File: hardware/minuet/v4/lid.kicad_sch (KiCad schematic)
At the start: 13 parts, among them J9 B2B-XH-A, U6 DRV8876PWP

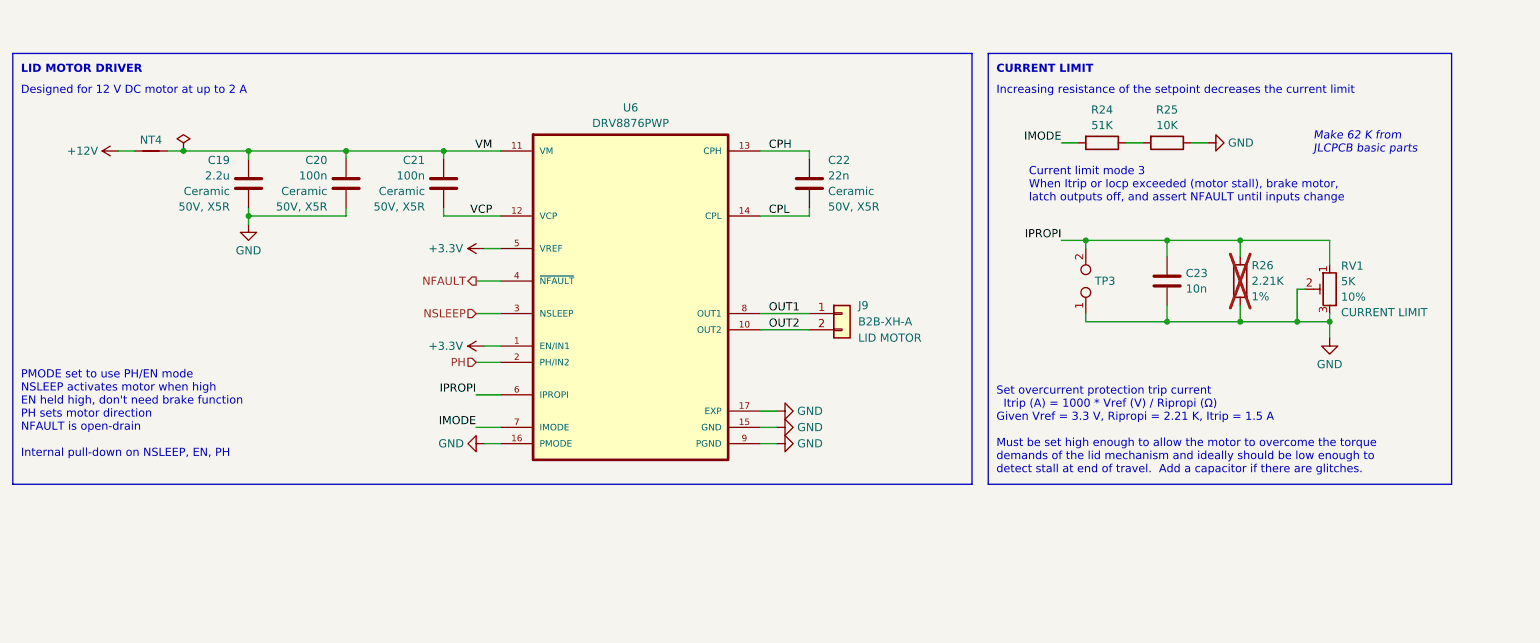
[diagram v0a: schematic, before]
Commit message: First draft of Minuet v4 fan controller board
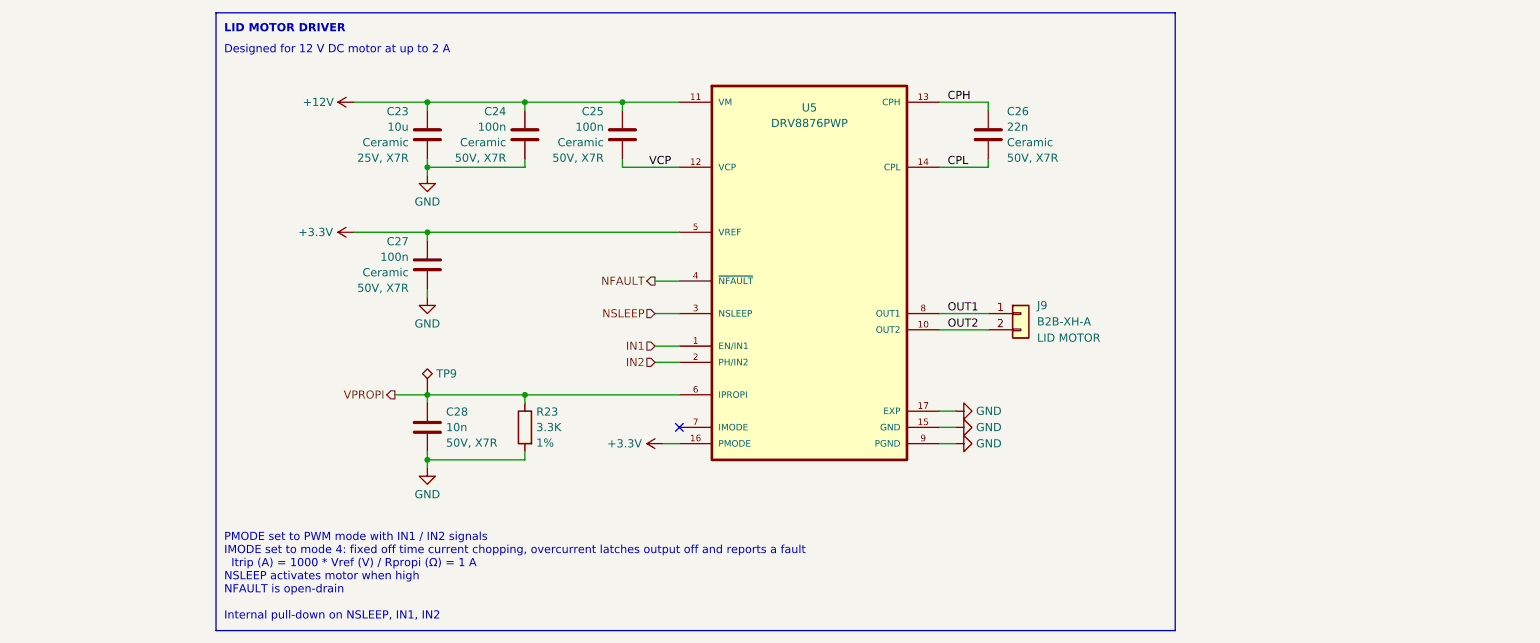
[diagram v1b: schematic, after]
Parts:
- removed C19: 2.2u, Capacitor_SMD:C_0805_2012Metric, symbol Device:C
- removed NT4: NetTie_2, Generic:NetTie-2_SMD_Pad1.0mm, symbol Device:NetTie_2
- removed R24: 51K, Resistor_SMD:R_0603_1608Metric, symbol Device:R
- removed R25: 10K, Resistor_SMD:R_0603_1608Metric, symbol Device:R
- removed RV1: 5K, 3362P-1-502LF:TRIM_3362P-1-502LF, symbol Device:R_Potentiometer_Trim
- removed TP3: TestPoint_2Pole, TestPoint:TestPoint_2Pads_Pitch2.54mm_Drill0.8mm, symbol Connector:TestPoint_2Pole
- added C23: 10u, Capacitor_SMD:C_1210_3225Metric, symbol Device:C
- added C27: 100n, Capacitor_SMD:C_0603_1608Metric, symbol Device:C
- added TP9: TestPoint_Alt, TestPoint:TestPoint_Pad_D1.0mm, symbol Connector:TestPoint_Alt
- C24: renamed from C20; Rating 50V, X5R -> 50V, X7R
- C25: renamed from C21; Rating 50V, X5R -> 50V, X7R
- C26: renamed from C22; Rating 50V, X5R -> 50V, X7R
- C28: renamed from C23; Rating 50V, X5R -> 50V, X7R
- R23: renamed from R26; value 2.21K -> 3.3K; LCSC (none) -> C22978; now fitted; now in the parts list
- U5: renamed from U6; MANUFACTURER (none) -> Texas Instruments; MAXIMUM_PACKAGE_HEIGHT (none) -> 1.2mm; PACKAGE (none) -> HTSSOP-16 Texas Instruments; PARTREV (none) -> E; STANDARD (none) -> Manufacturer Recommendations
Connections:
- net VM is gone; now on net +12V: C24.1, C25.1, U5.11 (VM)
- net +12V: now also C23.1
- net +3.3V: now also U5.16 (PMODE), C27.1; no longer U5.1 (EN/IN1)
- net GND: now also C23.2, C27.2; no longer U5.16 (PMODE)
- net IMODE: no longer names the net of U5.7 (IMODE)
- net IPROPI renamed VPROPI
- net VPROPI: now also TP9.1
- net PH renamed IN2
- new net IN1: U5.1 (EN/IN1)
- no-connect marks 0 -> 1
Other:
- note added: "PMODE set to PWM mode with IN1 / IN2 signals IMODE set to mode 4: fixed off time current chopping, overcurrent latches output off and reports a fault Itrip (A) = 1000 * Vref (V) / Rpropi (Ω) = 1 A NSLEEP activates motor when high NFAULT is open-drain Internal pull-down on NSLEEP, IN1, IN2"
- note removed: "CURRENT LIMIT"
- note removed: "Current limit mode 3 When Itrip or Iocp exceeded (motor stall), brake motor, latch outputs off, and assert NFAULT until inputs change"
- note removed: "Increasing resistance of the setpoint decreases the current limit"
- note removed: "Make 62 K from JLCPCB basic parts"
- note removed: "PMODE set to use PH/EN mode NSLEEP activates motor when high EN held high, don't need brake function PH sets motor direction NFAULT is open-drain Internal pull-down on NSLEEP, EN, PH"
- note removed: "Set overcurrent protection trip current Itrip (A) = 1000 * Vref (V) / Ripropi (Ω) Given Vref = 3.3 V, Ripropi = 2.21 K, Itrip = 1.5 A Must be set high enough to allow the motor to overcome the torque demands of the lid mechanism and ideally should be low enough to detect stall at end of travel. Add a capacitor if there are glitches."
- company: (none) -> Brown Studios LLC
- moved on the sheet: C24, C25, C26, C28, J9, U5

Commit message: Second draft of Minuet v4 main board.
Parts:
- renumbered C23 to C24, C24 to C25, C25 to C26, C26 to C27, C27 to C28, C28 to C29, R23 to R24, TP9 to TP8
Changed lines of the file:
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@@
 		(on_board yes)
 		(dnp no)
-		(property "Reference" "#PWR058"
+		(property "Reference" "#PWR060"
 			(at 140.97 118.11 0)
 			(effects
@@
 			(project "minuet"
 				(path "/5bd7983a-3caa-4bb2-9dc5-1af533f31e50/713a3115-7b9d-4f98-8679-6fd4cf9d6fa9"
-					(reference "#PWR058")
+					(reference "#PWR060")
 					(unit 1)
 				)
@@
 		(dnp no)
 		(fields_autoplaced yes)
-		(property "Reference" "#PWR055"
+		(property "Reference" "#PWR057"
 			(at 100.33 101.6 0)
 			(effects
@@
 			(project "minuet"
 				(path "/5bd7983a-3caa-4bb2-9dc5-1af533f31e50/713a3115-7b9d-4f98-8679-6fd4cf9d6fa9"
-					(reference "#PWR055")
+					(reference "#PWR057")
 					(unit 1)
 				)
@@
 		(on_board yes)
 		(dnp no)
-		(property "Reference" "C24"
+		(property "Reference" "C25"
 			(at 112.649 66.2135 0)
 			(effects
@@
 			(project "minuet"
 				(path "/5bd7983a-3caa-4bb2-9dc5-1af533f31e50/713a3115-7b9d-4f98-8679-6fd4cf9d6fa9"
-					(reference "C24")
+					(reference "C25")
 					(unit 1)
 				)
@@
 		(dnp no)
 		(fields_autoplaced yes)
-		(property "Reference" "#PWR057"
+		(property "Reference" "#PWR059"
 			(at 189.23 115.57 0)
 			(effects
@@
 			(project "minuet"
 				(path "/5bd7983a-3caa-4bb2-9dc5-1af533f31e50/713a3115-7b9d-4f98-8679-6fd4cf9d6fa9"
-					(reference "#PWR057")
+					(reference "#PWR059")
 					(unit 1)
 				)
@@
 		(dnp no)
 		(fields_autoplaced yes)
-		(property "Reference" "TP9"
+		(property "Reference" "TP8"
 			(at 101.727 107.188 0)
 			(effects
@@
 			(project ""
 				(path "/5bd7983a-3caa-4bb2-9dc5-1af533f31e50/713a3115-7b9d-4f98-8679-6fd4cf9d6fa9"
-					(reference "TP9")
+					(reference "TP8")
 					(unit 1)
 				)
@@
 		(dnp no)
 		(fields_autoplaced yes)
-		(property "Reference" "C26"
+		(property "Reference" "C27"
 			(at 190.881 66.2135 0)
 			(effects
@@
 			(project "minuet"
 				(path "/5bd7983a-3caa-4bb2-9dc5-1af533f31e50/713a3115-7b9d-4f98-8679-6fd4cf9d6fa9"
-					(reference "C26")
+					(reference "C27")
 					(unit 1)
 				)
@@
 		(on_board yes)
 		(dnp no)
-		(property "Reference" "C25"
+		(property "Reference" "C26"
 			(at 127.889 66.2135 0)
 			(effects
@@
 			(project "minuet"
 				(path "/5bd7983a-3caa-4bb2-9dc5-1af533f31e50/713a3115-7b9d-4f98-8679-6fd4cf9d6fa9"
-					(reference "C25")
+					(reference "C26")
 					(unit 1)
 				)
@@
 		(on_board yes)
 		(dnp no)
-		(property "Reference" "C27"
+		(property "Reference" "C28"
 			(at 97.409 86.5335 0)
 			(effects
@@
 			(project "minuet"
 				(path "/5bd7983a-3caa-4bb2-9dc5-1af533f31e50/713a3115-7b9d-4f98-8679-6fd4cf9d6fa9"
-					(reference "C27")
+					(reference "C28")
 					(unit 1)
 				)
@@
 		(dnp no)
 		(fields_autoplaced yes)
-		(property "Reference" "#PWR053"
+		(property "Reference" "#PWR055"
 			(at 100.33 82.55 0)
 			(effects
@@
 			(project "minuet"
 				(path "/5bd7983a-3caa-4bb2-9dc5-1af533f31e50/713a3115-7b9d-4f98-8679-6fd4cf9d6fa9"
-					(reference "#PWR053")
+					(reference "#PWR055")
 					(unit 1)
 				)
@@
 		(dnp no)
 		(fields_autoplaced yes)
-		(property "Reference" "#PWR052"
+		(property "Reference" "#PWR054"
 			(at 92.71 64.77 0)
 			(effects
@@
 			(project "minuet"
 				(path "/5bd7983a-3caa-4bb2-9dc5-1af533f31e50/713a3115-7b9d-4f98-8679-6fd4cf9d6fa9"
-					(reference "#PWR052")
+					(reference "#PWR054")
 					(unit 1)
 				)
@@
 		(dnp no)
 		(fields_autoplaced yes)
-		(property "Reference" "#PWR060"
+		(property "Reference" "#PWR062"
 			(at 100.33 128.27 0)
 			(effects
@@
 			(project "minuet"
 				(path "/5bd7983a-3caa-4bb2-9dc5-1af533f31e50/713a3115-7b9d-4f98-8679-6fd4cf9d6fa9"
-					(reference "#PWR060")
+					(reference "#PWR062")
 					(unit 1)
 				)
@@
 		(dnp no)
 		(fields_autoplaced yes)
-		(property "Reference" "#PWR059"
+		(property "Reference" "#PWR061"
 			(at 189.23 118.11 0)
 			(effects
@@
 			(project "minuet"
 				(path "/5bd7983a-3caa-4bb2-9dc5-1af533f31e50/713a3115-7b9d-4f98-8679-6fd4cf9d6fa9"
-					(reference "#PWR059")
+					(reference "#PWR061")
 					(unit 1)
 				)
@@
 		(dnp no)
 		(fields_autoplaced yes)
-		(property "Reference" "#PWR056"
+		(property "Reference" "#PWR058"
 			(at 189.23 113.03 0)
 			(effects
@@
 			(project "minuet"
 				(path "/5bd7983a-3caa-4bb2-9dc5-1af533f31e50/713a3115-7b9d-4f98-8679-6fd4cf9d6fa9"
-					(reference "#PWR056")
+					(reference "#PWR058")
 					(unit 1)
 				)
@@
 		(on_board yes)
 		(dnp no)
-		(property "Reference" "R23"
+		(property "Reference" "R24"
 			(at 117.348 113.1457 0)
 			(effects
@@
 			(project "minuet"
 				(path "/5bd7983a-3caa-4bb2-9dc5-1af533f31e50/713a3115-7b9d-4f98-8679-6fd4cf9d6fa9"
-					(reference "R23")
+					(reference "R24")
 					(unit 1)
 				)
@@
 		(on_board yes)
 		(dnp no)
-		(property "Reference" "#PWR054"
+		(property "Reference" "#PWR056"
 			(at 92.71 85.09 0)
 			(effects
@@
 			(project "minuet"
 				(path "/5bd7983a-3caa-4bb2-9dc5-1af533f31e50/713a3115-7b9d-4f98-8679-6fd4cf9d6fa9"
-					(reference "#PWR054")
+					(reference "#PWR056")
 					(unit 1)
 				)
@@
 		(on_board yes)
 		(dnp no)
-		(property "Reference" "C23"
+		(property "Reference" "C24"
 			(at 97.409 66.2135 0)
 			(effects
@@
 			(project "minuet"
 				(path "/5bd7983a-3caa-4bb2-9dc5-1af533f31e50/713a3115-7b9d-4f98-8679-6fd4cf9d6fa9"
-					(reference "C23")
+					(reference "C24")
 					(unit 1)
 				)
@@
 		(on_board yes)
 		(dnp no)
-		(property "Reference" "C28"
+		(property "Reference" "C29"
 			(at 103.251 113.1457 0)
 			(effects
@@
 			(project "minuet"
 				(path "/5bd7983a-3caa-4bb2-9dc5-1af533f31e50/713a3115-7b9d-4f98-8679-6fd4cf9d6fa9"
-					(reference "C28")
-					(unit 1)
-				)
+					(reference "C29")
+					(unit 1)
+				)

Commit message: Prepare main board for fabrication
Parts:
- renumbered TP8 to TP9
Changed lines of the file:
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@@
 		(on_board yes)
 		(dnp no)
-		(property "Reference" "#PWR060"
+		(property "Reference" "#PWR061"
 			(at 140.97 118.11 0)
 			(effects
@@
 			(project "minuet"
 				(path "/5bd7983a-3caa-4bb2-9dc5-1af533f31e50/713a3115-7b9d-4f98-8679-6fd4cf9d6fa9"
-					(reference "#PWR060")
+					(reference "#PWR061")
 					(unit 1)
 				)
@@
 		(dnp no)
 		(fields_autoplaced yes)
-		(property "Reference" "#PWR057"
+		(property "Reference" "#PWR058"
 			(at 100.33 101.6 0)
 			(effects
@@
 			(project "minuet"
 				(path "/5bd7983a-3caa-4bb2-9dc5-1af533f31e50/713a3115-7b9d-4f98-8679-6fd4cf9d6fa9"
-					(reference "#PWR057")
+					(reference "#PWR058")
 					(unit 1)
 				)
@@
 		(dnp no)
 		(fields_autoplaced yes)
-		(property "Reference" "#PWR059"
+		(property "Reference" "#PWR060"
 			(at 189.23 115.57 0)
 			(effects
@@
 			(project "minuet"
 				(path "/5bd7983a-3caa-4bb2-9dc5-1af533f31e50/713a3115-7b9d-4f98-8679-6fd4cf9d6fa9"
-					(reference "#PWR059")
+					(reference "#PWR060")
 					(unit 1)
 				)
@@
 		(dnp no)
 		(fields_autoplaced yes)
-		(property "Reference" "TP8"
+		(property "Reference" "TP9"
 			(at 101.727 107.188 0)
 			(effects
@@
 			(project ""
 				(path "/5bd7983a-3caa-4bb2-9dc5-1af533f31e50/713a3115-7b9d-4f98-8679-6fd4cf9d6fa9"
-					(reference "TP8")
+					(reference "TP9")
 					(unit 1)
 				)
@@
 		(dnp no)
 		(fields_autoplaced yes)
-		(property "Reference" "#PWR055"
+		(property "Reference" "#PWR056"
 			(at 100.33 82.55 0)
 			(effects
@@
 			(project "minuet"
 				(path "/5bd7983a-3caa-4bb2-9dc5-1af533f31e50/713a3115-7b9d-4f98-8679-6fd4cf9d6fa9"
-					(reference "#PWR055")
+					(reference "#PWR056")
 					(unit 1)
 				)
@@
 		(dnp no)
 		(fields_autoplaced yes)
-		(property "Reference" "#PWR054"
+		(property "Reference" "#PWR055"
 			(at 92.71 64.77 0)
 			(effects
@@
 			(project "minuet"
 				(path "/5bd7983a-3caa-4bb2-9dc5-1af533f31e50/713a3115-7b9d-4f98-8679-6fd4cf9d6fa9"
-					(reference "#PWR054")
+					(reference "#PWR055")
 					(unit 1)
 				)
@@
 		(dnp no)
 		(fields_autoplaced yes)
-		(property "Reference" "#PWR062"
+		(property "Reference" "#PWR063"
 			(at 100.33 128.27 0)
 			(effects
@@
 			(project "minuet"
 				(path "/5bd7983a-3caa-4bb2-9dc5-1af533f31e50/713a3115-7b9d-4f98-8679-6fd4cf9d6fa9"
-					(reference "#PWR062")
+					(reference "#PWR063")
 					(unit 1)
 				)
@@
 		(dnp no)
 		(fields_autoplaced yes)
-		(property "Reference" "#PWR061"
+		(property "Reference" "#PWR062"
 			(at 189.23 118.11 0)
 			(effects
@@
 			(project "minuet"
 				(path "/5bd7983a-3caa-4bb2-9dc5-1af533f31e50/713a3115-7b9d-4f98-8679-6fd4cf9d6fa9"
-					(reference "#PWR061")
+					(reference "#PWR062")
 					(unit 1)
 				)
@@
 		(dnp no)
 		(fields_autoplaced yes)
-		(property "Reference" "#PWR058"
+		(property "Reference" "#PWR059"
 			(at 189.23 113.03 0)
 			(effects
@@
 			(project "minuet"
 				(path "/5bd7983a-3caa-4bb2-9dc5-1af533f31e50/713a3115-7b9d-4f98-8679-6fd4cf9d6fa9"
-					(reference "#PWR058")
+					(reference "#PWR059")
 					(unit 1)
 				)
@@
 		(on_board yes)
 		(dnp no)
-		(property "Reference" "#PWR056"
+		(property "Reference" "#PWR057"
 			(at 92.71 85.09 0)
 			(effects
@@
 			(project "minuet"
 				(path "/5bd7983a-3caa-4bb2-9dc5-1af533f31e50/713a3115-7b9d-4f98-8679-6fd4cf9d6fa9"
-					(reference "#PWR056")
-					(unit 1)
-				)
+					(reference "#PWR057")
+					(unit 1)
+				)
